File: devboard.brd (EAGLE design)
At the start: 31.5 x 55 mm, 23 parts, among them Q1 CRYSTALX22, X1 MICROMATCH-8

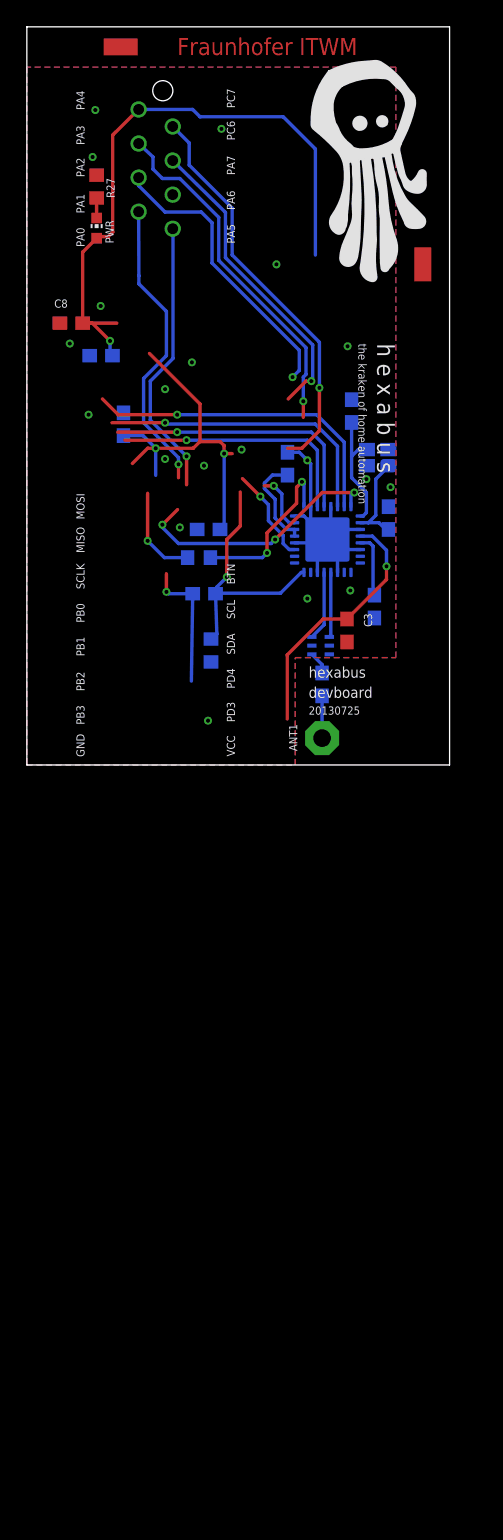
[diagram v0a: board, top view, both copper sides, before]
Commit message: added eeprom for storing mac address and 2x13 pin connector
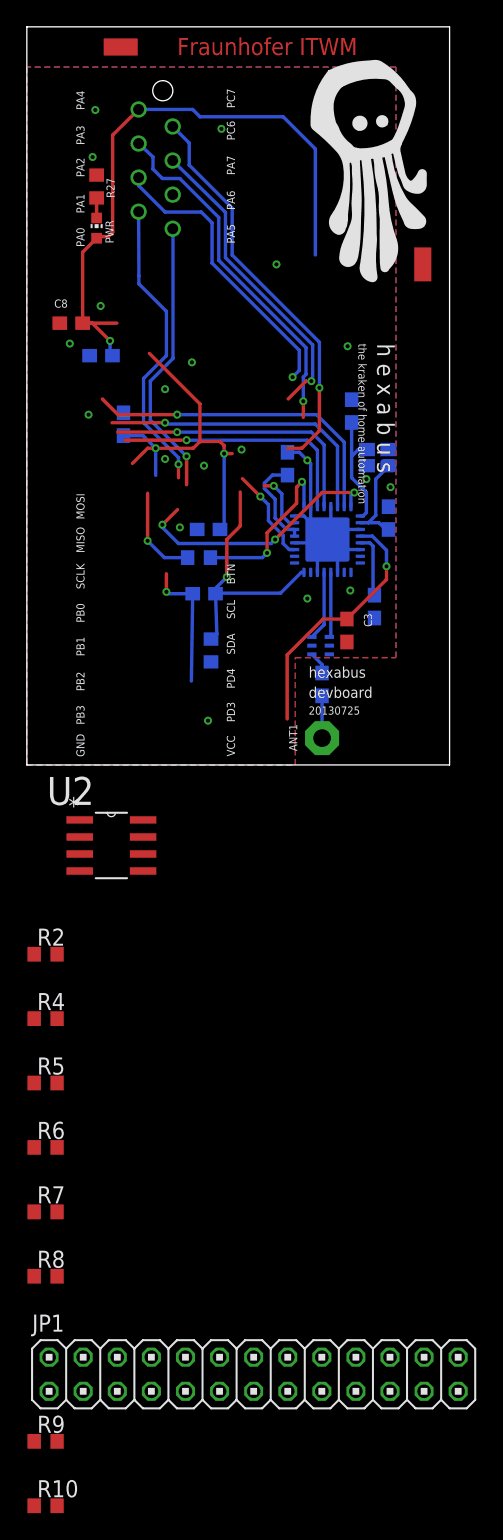
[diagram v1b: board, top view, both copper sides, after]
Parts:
- added JP1: (no value), pinhead:2X13
- added R10, R9: 4k7, rcl:R0603
- added R2, R4, R5, R6, R7, R8: 0R, rcl:R0603
- added U2: 24LC32A/SN, hexabus:SOIC127P600X175-8N
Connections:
- new net N$10: R5.1, R8.2, U2.3
- new net N$4: R2.1, R6.2, U2.1
- new net N$9: R4.1, R7.2, U2.2
- new net SCL: JP1.5, R10.1, U2.6
- new net SDA: JP1.3, R9.1, U2.5
- net AT_RST: now also JP1.16
- net GND: now also JP1.14, JP1.20, JP1.25, JP1.6, JP1.9, R6.1, R7.1, R8.1, U2.4, U2.7
- net IRQ: now also JP1.15
- net MISO: now also JP1.21
- net MOSI: now also JP1.19
- net SCLK: now also JP1.23
- net SEL1: now also JP1.24
- net SLP_TR: now also JP1.18
- net VCC: now also JP1.1, R10.2, R2.2, R4.2, R5.2, R9.2, U2.8
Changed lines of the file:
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@@
 </element>
 <element name="U$1" library="artwork" package="HEXAKRAKE" value="HEXAKRAKE" x="21.2" y="36.1"/>
+<element name="U2" library="hexabus" package="SOIC127P600X175-8N" value="24LC32A/SN" x="6.3" y="-6">
+<attribute name="PACKAGE" value="SOIC-8" x="6.3" y="-6" size="1.778" layer="27" display="off"/>
+<attribute name="OC_NEWARK" value="33C2976" x="6.3" y="-6" size="1.778" layer="27" display="off"/>
+<attribute name="MPN" value="24LC32A/SN" x="6.3" y="-6" size="1.778" layer="27" display="off"/>
+<attribute name="SUPPLIER" value="Microchip" x="6.3" y="-6" size="1.778" layer="27" display="off"/>
+<attribute name="OC_FARNELL" value="9758003" x="6.3" y="-6" size="1.778" layer="27" display="off"/>
+</element>
+<element name="R2" library="rcl" package="R0603" value="0R" x="1.4" y="-14.1"/>
+<element name="R4" library="rcl" package="R0603" value="0R" x="1.4" y="-18.9"/>
+<element name="R5" library="rcl" package="R0603" value="0R" x="1.4" y="-23.7"/>
+<element name="R6" library="rcl" package="R0603" value="0R" x="1.4" y="-28.5"/>
+<element name="R7" library="rcl" package="R0603" value="0R" x="1.4" y="-33.3"/>
+<element name="R8" library="rcl" package="R0603" value="0R" x="1.4" y="-38.1"/>
+<element name="JP1" library="pinhead" package="2X13" value="" x="16.9" y="-45.4"/>
+<element name="R9" library="rcl" package="R0603" value="4k7" x="1.4" y="-50.4"/>
+<element name="R10" library="rcl" package="R0603" value="4k7" x="1.4" y="-55.2"/>
 </elements>
 <signals>
@@
 <via x="10.3" y="22.8" extent="1-16" drill="0.3"/>
 <via x="24.1" y="13" extent="1-16" drill="0.3"/>
+<contactref element="U2" pad="4"/>
+<contactref element="U2" pad="7"/>
+<contactref element="R8" pad="1"/>
+<contactref element="R7" pad="1"/>
+<contactref element="R6" pad="1"/>
+<contactref element="JP1" pad="25"/>
+<contactref element="JP1" pad="9"/>
+<contactref element="JP1" pad="6"/>
+<contactref element="JP1" pad="14"/>
+<contactref element="JP1" pad="20"/>
 <wire x1="10.87" y1="42.495" x2="14.5" y2="47.4" width="0" layer="19" extent="1-1"/>
 <wire x1="5.2" y1="43.95" x2="10.87" y2="42.495" width="0" layer="19" extent="1-1"/>
@@
 <wire x1="13.72" y1="7.68" x2="21.2398" y2="8.8914" width="0" layer="19" extent="16-16"/>
 <wire x1="13.5" y1="3.3" x2="13.72" y2="7.68" width="0" layer="19" extent="16-16"/>
+<wire x1="8.6622" y1="-5.365" x2="13.5" y2="3.3" width="0" layer="19" extent="1-1"/>
+<wire x1="3.9378" y1="-7.905" x2="8.6622" y2="-5.365" width="0" layer="19" extent="1-1"/>
+<wire x1="0.55" y1="-28.5" x2="3.9378" y2="-7.905" width="0" layer="19" extent="1-1"/>
+<wire x1="0.55" y1="-33.3" x2="0.55" y2="-28.5" width="0" layer="19" extent="1-1"/>
+<wire x1="0.55" y1="-38.1" x2="0.55" y2="-33.3" width="0" layer="19" extent="1-1"/>
+<wire x1="6.74" y1="-44.13" x2="0.55" y2="-38.1" width="0" layer="19" extent="1-1"/>
+<wire x1="11.82" y1="-46.67" x2="6.74" y2="-44.13" width="0" layer="19" extent="1-1"/>
+<wire x1="16.9" y1="-44.13" x2="11.82" y2="-46.67" width="0" layer="19" extent="1-1"/>
+<wire x1="24.52" y1="-44.13" x2="16.9" y2="-44.13" width="0" layer="19" extent="1-1"/>
+<wire x1="32.14" y1="-46.67" x2="24.52" y2="-44.13" width="0" layer="19" extent="1-1"/>
 </signal>
 <signal name="IRQ">
@@
 <via x="18.5" y="16.8" extent="1-16" drill="0.3"/>
 <via x="10.1" y="17.9" extent="1-16" drill="0.3"/>
+<contactref element="JP1" pad="15"/>
+<wire x1="18.2" y1="16.5" x2="19.44" y2="-46.67" width="0" layer="19" extent="16-16"/>
 </signal>
 <signal name="MISO">
@@
 <wire x1="11.2" y1="24.8" x2="21.2" y2="24.8" width="0.254" layer="16"/>
 <via x="11.2" y="24.8" extent="1-16" drill="0.3"/>
+<contactref element="JP1" pad="21"/>
+<wire x1="27.06" y1="-46.67" x2="22.15" y2="19.25" width="0" layer="19" extent="16-16"/>
 </signal>
 <signal name="MOSI">
@@
 <wire x1="10.3" y1="25.5" x2="10.4" y2="25.4" width="0.254" layer="16"/>
 <via x="10.3" y="25.5" extent="1-16" drill="0.3"/>
+<contactref element="JP1" pad="19"/>
+<wire x1="24.52" y1="-46.67" x2="23.15" y2="19.25" width="0" layer="19" extent="16-16"/>
 </signal>
 <signal name="SEL1">
@@
 <wire x1="11.2" y1="26.1" x2="21.6" y2="26.1" width="0.254" layer="16"/>
 <via x="11.2" y="26.1" extent="1-16" drill="0.3"/>
+<contactref element="JP1" pad="24"/>
+<wire x1="29.6" y1="-44.13" x2="23.65" y2="19.25" width="0" layer="19" extent="16-16"/>
 </signal>
 <signal name="SLP_TR">
@@
 <wire x1="19.1" y1="16.5" x2="19.1" y2="17.1" width="0.254" layer="16"/>
 <via x="17.4" y="20" extent="1-16" drill="0.3"/>
+<contactref element="JP1" pad="18"/>
+<wire x1="21.98" y1="-44.13" x2="19.95" y2="16.05" width="0" layer="19" extent="16-16"/>
 </signal>
 <signal name="N$1">
@@
 <wire x1="14.9" y1="16.8" x2="15.9" y2="17.8" width="0.254" layer="1"/>
 <wire x1="15.9" y1="17.8" x2="15.9" y2="20.33725625" width="0.254" layer="1"/>
+<contactref element="JP1" pad="16"/>
+<wire x1="13.72" y1="9.38" x2="19.44" y2="-44.13" width="0" layer="19" extent="16-16"/>
 </signal>
 <signal name="TCK">
@@
 <wire x1="11.9" y1="24.2" x2="20.9" y2="24.2" width="0.254" layer="16"/>
 <via x="11.9" y="24.2" extent="1-16" drill="0.3"/>
+<contactref element="JP1" pad="23"/>
+<wire x1="29.6" y1="-46.67" x2="21.65" y2="19.25" width="0" layer="19" extent="16-16"/>
 </signal>
 <signal name="N$28">
@@
 <wire x1="7.2" y1="24.54" x2="8.66" y2="24.54" width="0.254" layer="16"/>
 <wire x1="8.66" y1="24.54" x2="9.6" y2="23.6" width="0.254" layer="16"/>
-<wire x1="15.2999" y1="23.2" x2="17.6999" y2="20.8" width="0" layer="19" extent="1-1"/>
+<contactref element="U2" pad="8"/>
+<contactref element="U2" pad="8"/>
+<contactref element="R5" pad="2"/>
+<contactref element="R4" pad="2"/>
+<contactref element="R2" pad="2"/>
+<contactref element="JP1" pad="1"/>
+<contactref element="R9" pad="2"/>
+<contactref element="R10" pad="2"/>
+<wire x1="2.25" y1="-50.4" x2="2.25" y2="-55.2" width="0" layer="19" extent="1-1"/>
+<wire x1="1.66" y1="-46.67" x2="2.25" y2="-50.4" width="0" layer="19" extent="1-1"/>
+<wire x1="2.25" y1="-23.7" x2="1.66" y2="-46.67" width="0" layer="19" extent="1-1"/>
+<wire x1="2.25" y1="-18.9" x2="2.25" y2="-23.7" width="0" layer="19" extent="1-1"/>
+<wire x1="2.25" y1="-14.1" x2="2.25" y2="-18.9" width="0" layer="19" extent="1-1"/>
+<wire x1="8.6622" y1="-4.095" x2="2.25" y2="-14.1" width="0" layer="19" extent="1-1"/>
+<wire x1="12.26" y1="6.25" x2="8.6622" y2="-4.095" width="0" layer="19" extent="1-16"/>
+<wire x1="14.39" y1="17.55" x2="10.4" y2="14.25" width="0" layer="19" extent="1-16"/>
 <wire x1="6.38" y1="30.5" x2="9.1331" y2="30.6669" width="0" layer="19" extent="1-16"/>
+<wire x1="17.6999" y1="20.8" x2="15.2999" y2="23.2" width="0" layer="19" extent="1-1"/>
 <wire x1="24.85" y1="17.05" x2="19.95" y2="18.05" width="0" layer="19" extent="16-16"/>
-<wire x1="10.4" y1="14.25" x2="14.39" y2="17.55" width="0" layer="19" extent="1-16"/>
+</signal>
+<signal name="SDA">
+<contactref element="U2" pad="5"/>
+<contactref element="JP1" pad="3"/>
+<contactref element="R9" pad="1"/>
+<wire x1="4.2" y1="-46.67" x2="0.55" y2="-50.4" width="0" layer="19" extent="1-1"/>
+<wire x1="8.6622" y1="-7.905" x2="4.2" y2="-46.67" width="0" layer="19" extent="1-1"/>
+</signal>
+<signal name="SCL">
+<contactref element="U2" pad="6"/>
+<contactref element="JP1" pad="5"/>
+<contactref element="R10" pad="1"/>
+<wire x1="6.74" y1="-46.67" x2="0.55" y2="-55.2" width="0" layer="19" extent="1-1"/>
+<wire x1="8.6622" y1="-6.635" x2="6.74" y2="-46.67" width="0" layer="19" extent="1-1"/>
+</signal>
+<signal name="N$4">
+<contactref element="U2" pad="1"/>
+<contactref element="R2" pad="1"/>
+<contactref element="R6" pad="2"/>
+<wire x1="0.55" y1="-14.1" x2="2.25" y2="-28.5" width="0" layer="19" extent="1-1"/>
+<wire x1="3.9378" y1="-4.095" x2="0.55" y2="-14.1" width="0" layer="19" extent="1-1"/>
+</signal>
+<signal name="N$9">
+<contactref element="U2" pad="2"/>
+<contactref element="R4" pad="1"/>
+<contactref element="R7" pad="2"/>
+<wire x1="0.55" y1="-18.9" x2="2.25" y2="-33.3" width="0" layer="19" extent="1-1"/>
+<wire x1="3.9378" y1="-5.365" x2="0.55" y2="-18.9" width="0" layer="19" extent="1-1"/>
+</signal>
+<signal name="N$10">
+<contactref element="U2" pad="3"/>
+<contactref element="R5" pad="1"/>
+<contactref element="R8" pad="2"/>
+<wire x1="0.55" y1="-23.7" x2="2.25" y2="-38.1" width="0" layer="19" extent="1-1"/>
+<wire x1="3.9378" y1="-6.635" x2="0.55" y2="-23.7" width="0" layer="19" extent="1-1"/>
 </signal>
 </signals>
